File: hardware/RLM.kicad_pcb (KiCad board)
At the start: 2 copper layers, 88.9 x 59.1 mm, 28 parts, among them J1 Conn_01x03, J2 Conn_01x03, SW1 SW_Push, SW2 SW_Push, U3 AP1117-33, U7 MCP2562-E-SN

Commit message: feat: trace board
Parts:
- C2, C4: value 104 -> 1u
- U1: renamed from ESP32; value U1 -> ESP32
- U2: renamed from NRF24L01; value U2 -> NRF24L01
- U4: renamed from GY-521; value U4 -> GY-521
- U5: renamed from GPS; value U5 -> BN-220
- U6: renamed from MicroSD Module; value U6 -> MicroSD Module
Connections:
- U4 pad 1: +3.3V -> +5V
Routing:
- net GND: track 0.00 -> 192.2 mm
- net +5V: track 0.00 -> 168.7 mm, vias 0 -> 1
- net SPI_MISO: track 0.00 -> 97.8 mm
- net SPI_SCK: track 0.00 -> 93.4 mm
- net CAN_TX: track 0.00 -> 87.9 mm, vias 0 -> 1
- net MPU_CAL: track 0.00 -> 77.2 mm, vias 0 -> 1
- net CAN_RX: track 0.00 -> 73.2 mm, vias 0 -> 1
- net +3.3V: track 0.00 -> 69.8 mm
- net SD_OFF: track 0.00 -> 66.5 mm
- net SPI_MOSI: track 0.00 -> 55.8 mm
- net NRF_VCC: track 0.00 -> 44.5 mm, vias 0 -> 1
- net GPS_RX: track 0.00 -> 42.2 mm
- net SD_CS: track 0.00 -> 40.1 mm
- net Net-(J2-Pin_1): track 0.00 -> 37.5 mm, vias 0 -> 2
- net V_SENSE: track 0.00 -> 37.0 mm
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
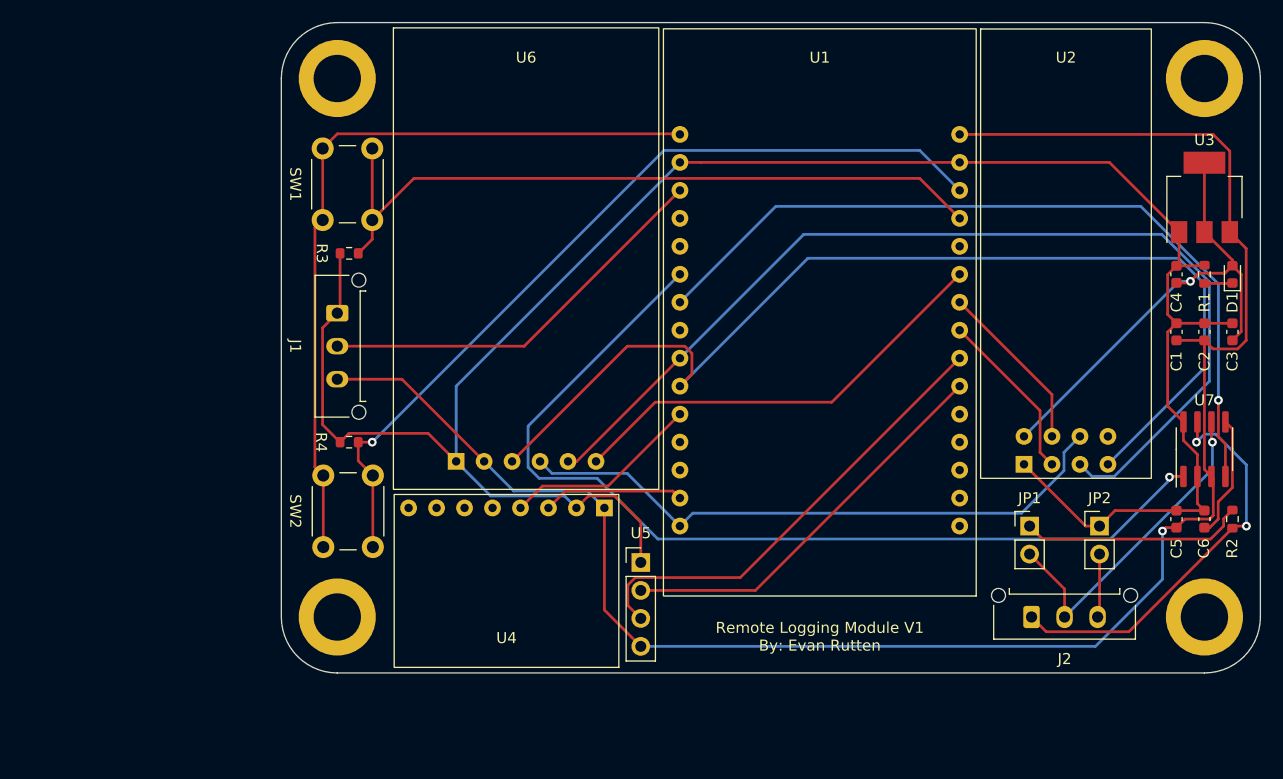
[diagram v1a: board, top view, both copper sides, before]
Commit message: fix: CAN resistances, ground pour, logo
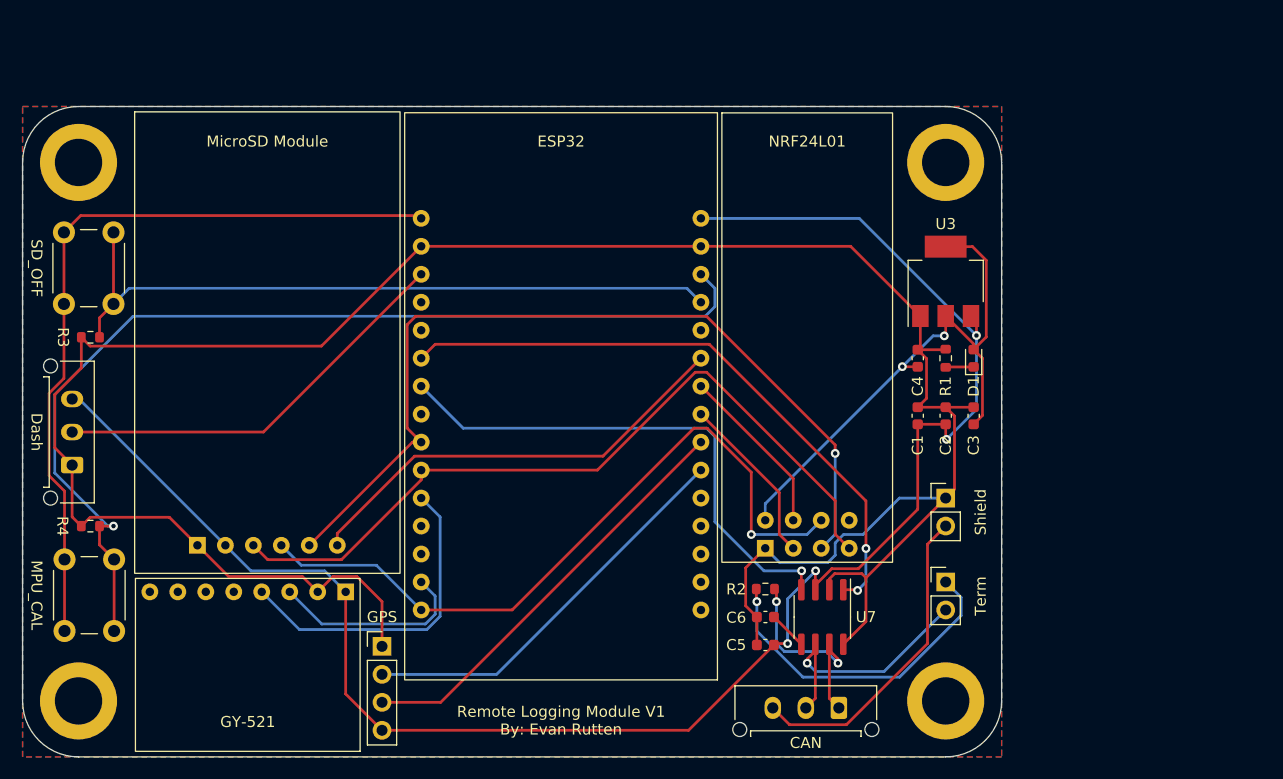
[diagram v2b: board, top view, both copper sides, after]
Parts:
- added G***: LOGO, GRC:GRCBanner, B.Cu at (122.6, 61.6)
- MicroSD Module: renamed from U6
- moved R2 42.9 mm to (141.1, 75.6), turned to 180 degrees
- moved C6 40.8 mm to (141.1, 78.1), turned to 180 degrees
- moved C5 39.0 mm to (141.1, 80.6), turned to 180 degrees
- moved U7 37.9 mm to (146.3, 78.1), turned to -90 degrees
- moved Dash 27.7 mm to (78.2, 64.3), turned to 90 degrees
- moved ESP32 24.7 mm to (122.6, 83.8)
- moved GPS 24.7 mm to (106.3, 80.8)
- moved MPU_CAL 24.7 mm to (77.5, 79.4)
- moved C1 24.7 mm to (154.9, 59.8)
- moved C2 24.7 mm to (157.5, 59.8)
- moved C4 24.7 mm to (154.9, 54.6)
- moved GY-521 24.7 mm to (94.1, 90.3)
- moved H1 24.7 mm to (157.5, 85.7)
- moved H2 24.7 mm to (78.7, 85.7)
- moved H3 24.7 mm to (157.5, 36.8)
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- renumbered J2 to CAN, J1 to Dash, U1 to ESP32, U5 to GPS, U4 to GY-521, SW2 to MPU_CAL, U2 to NRF24L01, SW1 to SD_OFF, JP2 to Shield, JP1 to Term
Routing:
- net CAN_TX: track 87.9 -> 56.6 mm, vias 1 -> 2
- net SPI_MISO: track 97.8 -> 70.6 mm
- net CAN_RX: track 73.2 -> 47.8 mm
- net Net-(J2-Pin_3): track 5.79 -> 29.1 mm
- net GND: track 192.2 -> 215.4 mm
- net Net-(J2-Pin_1): track 37.5 -> 19.5 mm
- net MPU_CAL: track 77.2 -> 92.5 mm
- net SPI_SCK: track 93.4 -> 79.2 mm, vias 0 -> 1
- net I2C_SDA: track 18.0 -> 29.6 mm
- net SPI_MOSI: track 55.8 -> 66.1 mm, vias 0 -> 1
- net Net-(JP1-A): track 20.4 -> 30.1 mm, vias 0 -> 1
- net GLV+: track 11.2 -> 3.51 mm
- net NRF_VCC: track 44.5 -> 51.7 mm, vias 1 -> 2
- net +5V: track 168.7 -> 161.7 mm, vias 1 -> 4
- net Net-(J2-Pin_2): track 30.3 -> 23.4 mm
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- added copper zone on B.Cu, net GND
- added copper zone on F.Cu, net GND

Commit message: feat: add gerbers
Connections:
- H1 pad 1: (no net) -> GND
- H2 pad 1: (no net) -> GND
- H3 pad 1: (no net) -> GND
- H4 pad 1: (no net) -> GND
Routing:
- net GND: track 215.4 -> 0.07 mm
- net +3.3V: track 70.5 -> 70.0 mm
